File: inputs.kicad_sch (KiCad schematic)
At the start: 31 parts, among them J3 MAP_Connector, U3 SP720

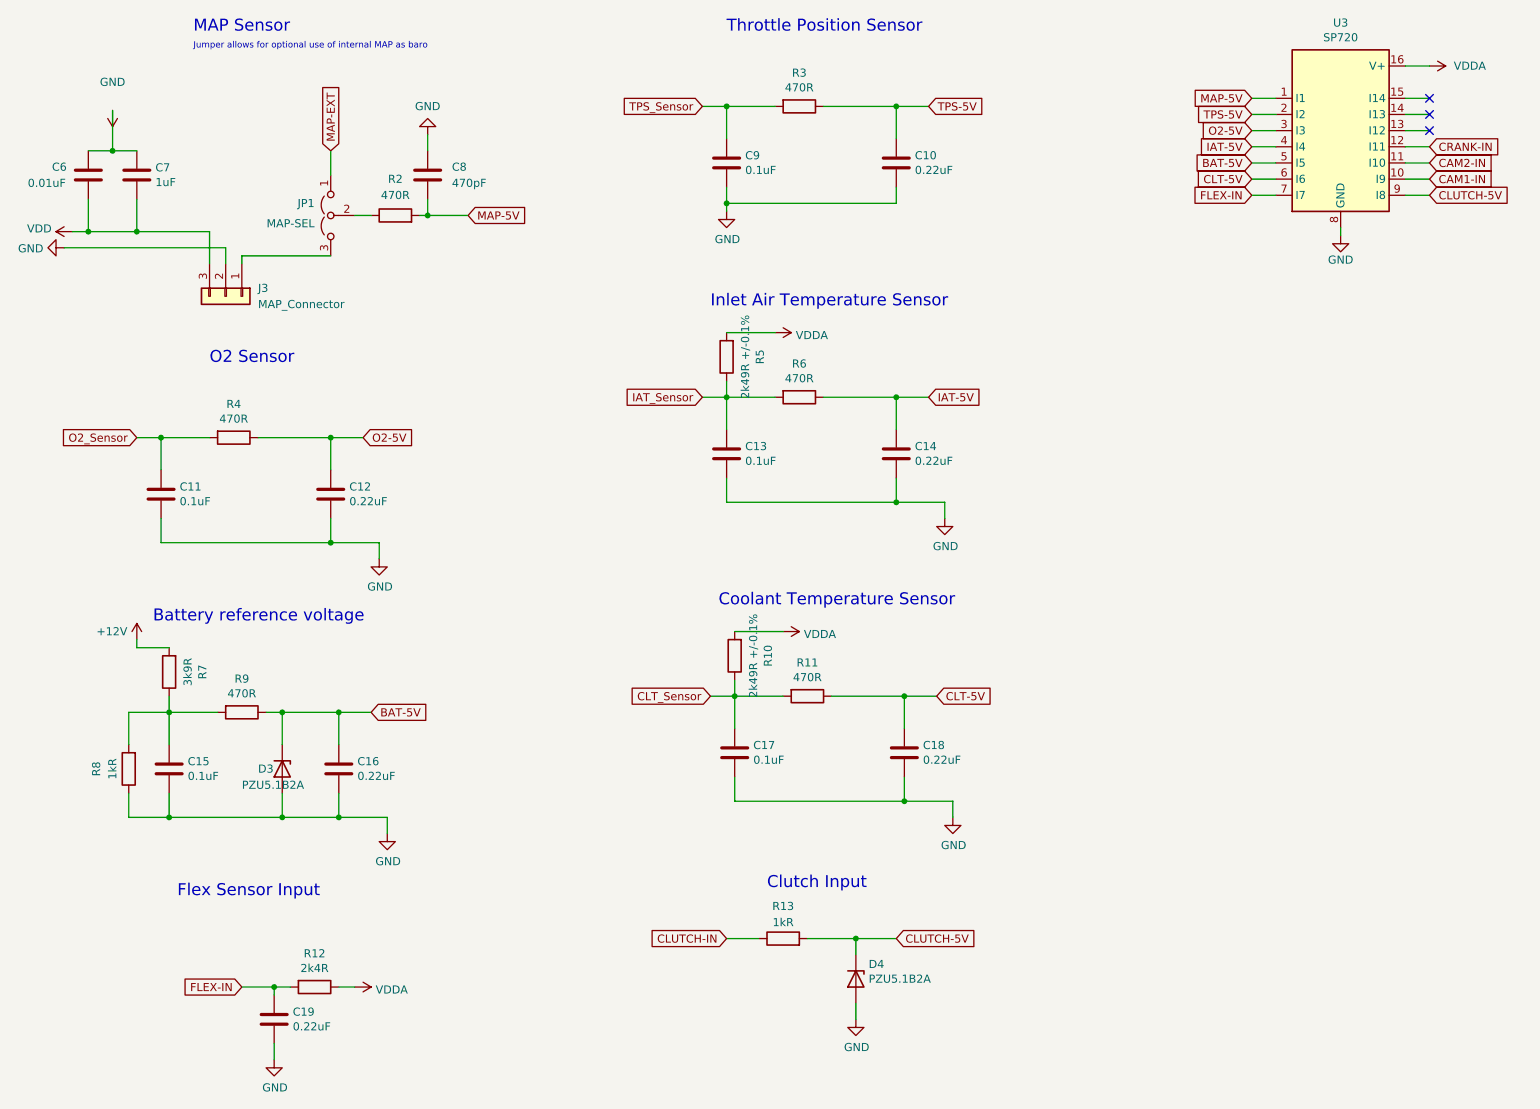
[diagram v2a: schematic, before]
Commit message: Swapped which angle sensors are connected to VR conditioners
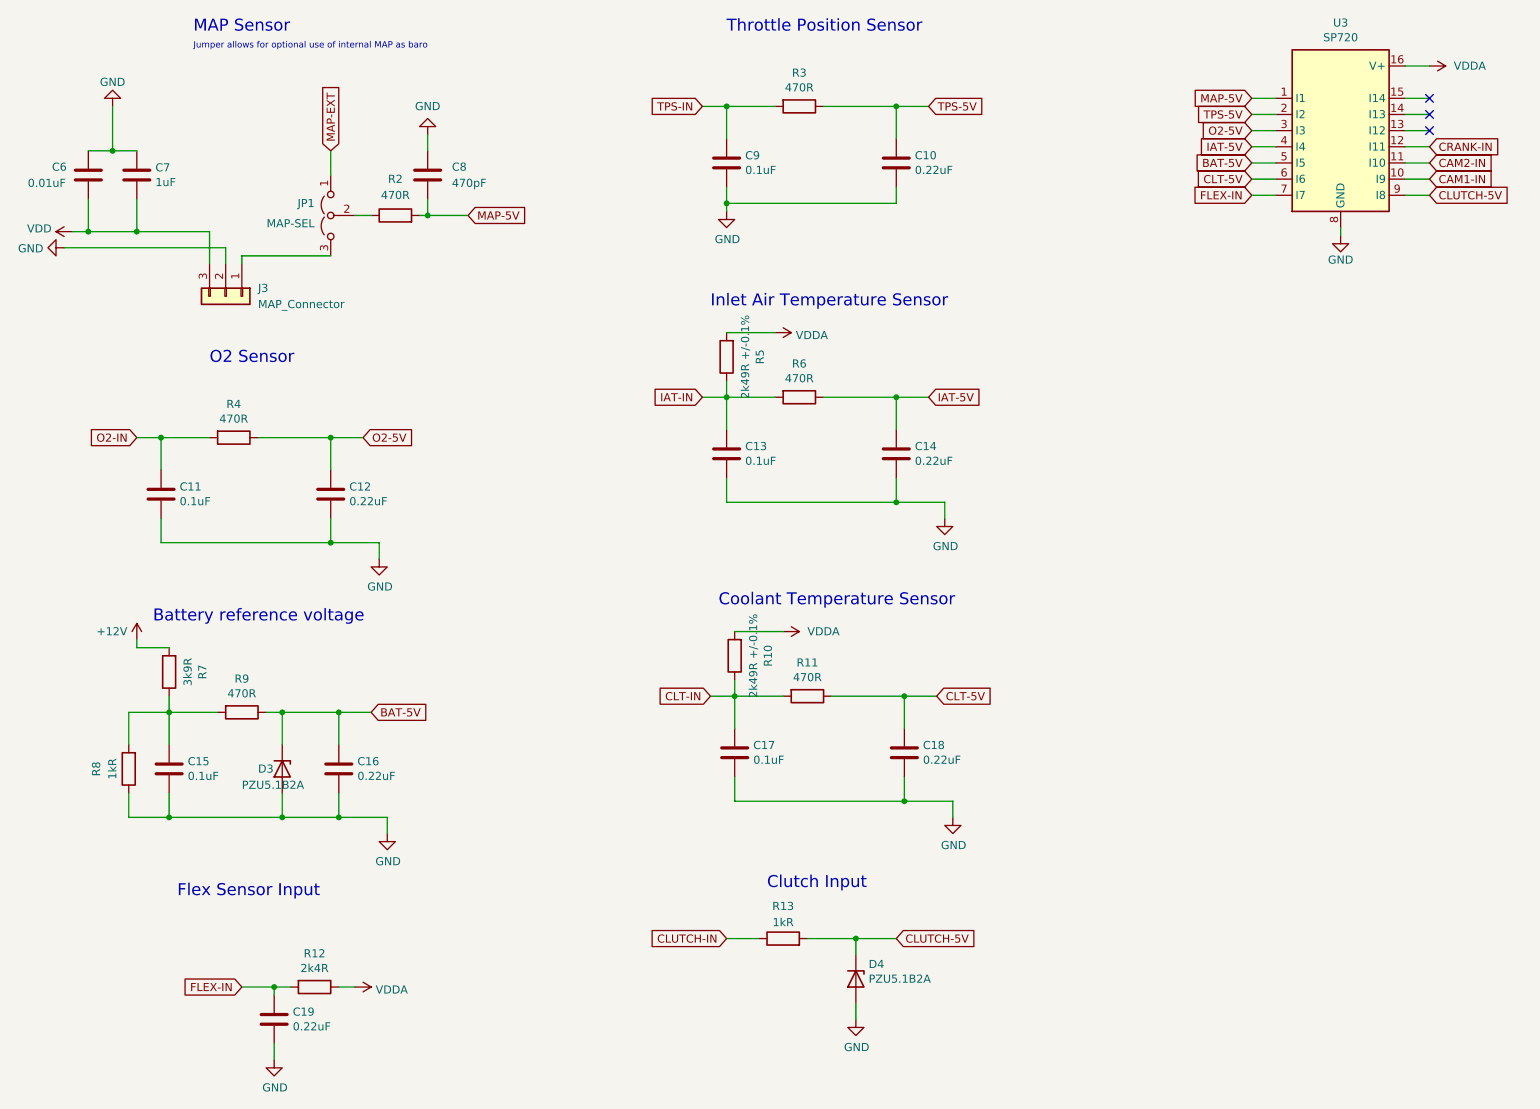
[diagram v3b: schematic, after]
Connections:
- net GND: now also C6.1, C7.1
- net VDD: no longer C6.1, C7.1, R10.2
- net VDDA: now also R10.2
- net CLT_Sensor renamed CLT-IN
- net IAT_Sensor renamed IAT-IN
- net O2_Sensor renamed O2-IN
- net TPS_Sensor renamed TPS-IN
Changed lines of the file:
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@@
     (stroke (width 0) (type default) (color 0 0 0 0))
   )
-  (wire (pts (xy 33.02 40.005) (xy 33.02 33.655))
+  (wire (pts (xy 33.02 33.02) (xy 33.02 40.005))
     (stroke (width 0) (type default) (color 0 0 0 0))
   )
@@
     )
   )
-  (global_label "CLT_Sensor" (shape input) (at 127 125.73 180) (fields_autoplaced)
+  (global_label "CLT-IN" (shape input) (at 127 125.73 180) (fields_autoplaced)
     (effects (font (size 1.27 1.27)) (justify right))
-    (property "Intersheet References" "${INTERSHEET_REFS}" (id 0) (at 0 0 0)
-      (effects (font (size 1.27 1.27)) hide)
+    (property "Intersheet References" "${INTERSHEET_REFS}" (id 0) (at 117.8136 125.6506 0)
+      (effects (font (size 1.27 1.27)) (justify right) hide)
     )
   )
@@
     )
   )
-  (global_label "IAT_Sensor" (shape input) (at 125.73 78.74 180) (fields_autoplaced)
+  (global_label "IAT-IN" (shape input) (at 125.73 78.74 180) (fields_autoplaced)
     (effects (font (size 1.27 1.27)) (justify right))
-    (property "Intersheet References" "${INTERSHEET_REFS}" (id 0) (at 0 0 0)
-      (effects (font (size 1.27 1.27)) hide)
+    (property "Intersheet References" "${INTERSHEET_REFS}" (id 0) (at 117.1483 78.6606 0)
+      (effects (font (size 1.27 1.27)) (justify right) hide)
     )
   )
@@
     )
   )
-  (global_label "TPS_Sensor" (shape input) (at 125.73 33.02 180) (fields_autoplaced)
+  (global_label "TPS-IN" (shape input) (at 125.73 33.02 180) (fields_autoplaced)
     (effects (font (size 1.27 1.27)) (justify right))
-    (property "Intersheet References" "${INTERSHEET_REFS}" (id 0) (at 0 0 0)
-      (effects (font (size 1.27 1.27)) hide)
+    (property "Intersheet References" "${INTERSHEET_REFS}" (id 0) (at 116.3621 32.9406 0)
+      (effects (font (size 1.27 1.27)) (justify right) hide)
     )
   )
@@
     )
   )
-  (global_label "O2_Sensor" (shape input) (at 36.83 85.09 180) (fields_autoplaced)
+  (global_label "O2-IN" (shape input) (at 36.83 85.09 180) (fields_autoplaced)
     (effects (font (size 1.27 1.27)) (justify right))
-    (property "Intersheet References" "${INTERSHEET_REFS}" (id 0) (at 0 0 0)
-      (effects (font (size 1.27 1.27)) hide)
+    (property "Intersheet References" "${INTERSHEET_REFS}" (id 0) (at 28.3693 85.0106 0)
+      (effects (font (size 1.27 1.27)) (justify right) hide)
     )
   )
@@
     (pin "2")
   )
-  (symbol (lib_id "power:VDD") (at 138.43 115.57 270) (unit 1)
-    (in_bom yes) (on_board yes)
-    (property "Reference" "#PWR0150" (id 0) (at 134.62 115.57 0)
-      (effects (font (size 1.27 1.27)) hide)
-    )
-    (property "Value" "VDDA" (id 1) (at 141.6812 116.0018 90)
-      (effects (font (size 1.27 1.27)) (justify left))
-    )
-    (property "Footprint" "" (id 2) (at 138.43 115.57 0)
-      (effects (font (size 1.27 1.27)) hide)
-    )
-    (property "Datasheet" "" (id 3) (at 138.43 115.57 0)
-      (effects (font (size 1.27 1.27)) hide)
-    )
-    (pin "1")
-  )
   (symbol (lib_id "Device:R") (at 53.34 128.27 270) (unit 1)
     (in_bom yes) (on_board yes)
@@
     (pin "1")
     (pin "2")
+  )
+  (symbol (lib_id "power:VDDA") (at 138.43 115.57 270) (unit 1)
+    (in_bom yes) (on_board yes) (fields_autoplaced)
+    (property "Reference" "#PWR0150" (id 0) (at 134.62 115.57 0)
+      (effects (font (size 1.27 1.27)) hide)
+    )
+    (property "Value" "VDDA" (id 1) (at 142.24 115.5699 90)
+      (effects (font (size 1.27 1.27)) (justify left))
+    )
+    (property "Footprint" "" (id 2) (at 138.43 115.57 0)
+      (effects (font (size 1.27 1.27)) hide)
+    )
+    (property "Datasheet" "" (id 3) (at 138.43 115.57 0)
+      (effects (font (size 1.27 1.27)) hide)
+    )
+    (pin "1")
   )
   (symbol (lib_id "Device:R") (at 77.47 50.165 90) (unit 1)
@@
     (pin "2")
   )
+  (symbol (lib_id "power:GND") (at 33.02 33.02 180) (unit 1)
+    (in_bom yes) (on_board yes)
+    (property "Reference" "#PWR0145" (id 0) (at 33.02 26.67 0)
+      (effects (font (size 1.27 1.27)) hide)
+    )
+    (property "Value" "GND" (id 1) (at 33.02 29.21 0))
+    (property "Footprint" "" (id 2) (at 33.02 33.02 0)
+      (effects (font (size 1.27 1.27)) hide)
+    )
+    (property "Datasheet" "" (id 3) (at 33.02 33.02 0)
+      (effects (font (size 1.27 1.27)) hide)
+    )
+    (pin "1")
+  )
   (symbol (lib_id "power:GND") (at 82.55 37.465 180) (unit 1)
     (in_bom yes) (on_board yes)
@@
     (pin "2")
   )
-  (symbol (lib_id "power:VDD") (at 33.02 33.655 180) (unit 1)
-    (in_bom yes) (on_board yes)
-    (property "Reference" "#PWR0145" (id 0) (at 33.02 27.305 0)
-      (effects (font (size 1.27 1.27)) hide)
-    )
-    (property "Value" "GND" (id 1) (at 33.02 29.21 0))
-    (property "Footprint" "" (id 2) (at 33.02 33.655 0)
-      (effects (font (size 1.27 1.27)) hide)
-    )
-    (property "Datasheet" "" (id 3) (at 33.02 33.655 0)
-      (effects (font (size 1.27 1.27)) hide)
-    )
-    (pin "1")
-  )
   (symbol (lib_id "Jumper:Jumper_3_Open") (at 67.31 50.165 90) (mirror x) (unit 1)
